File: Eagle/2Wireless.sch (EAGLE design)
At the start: 21 parts, among them IC1 TCA9517A, IC2 VREGLD1117, IC3 MB85RS2MTAPNF-G-BDERE1, IC4 24FC512, IC5 24FC512, U1 PHOTON_WITH_HEADERS

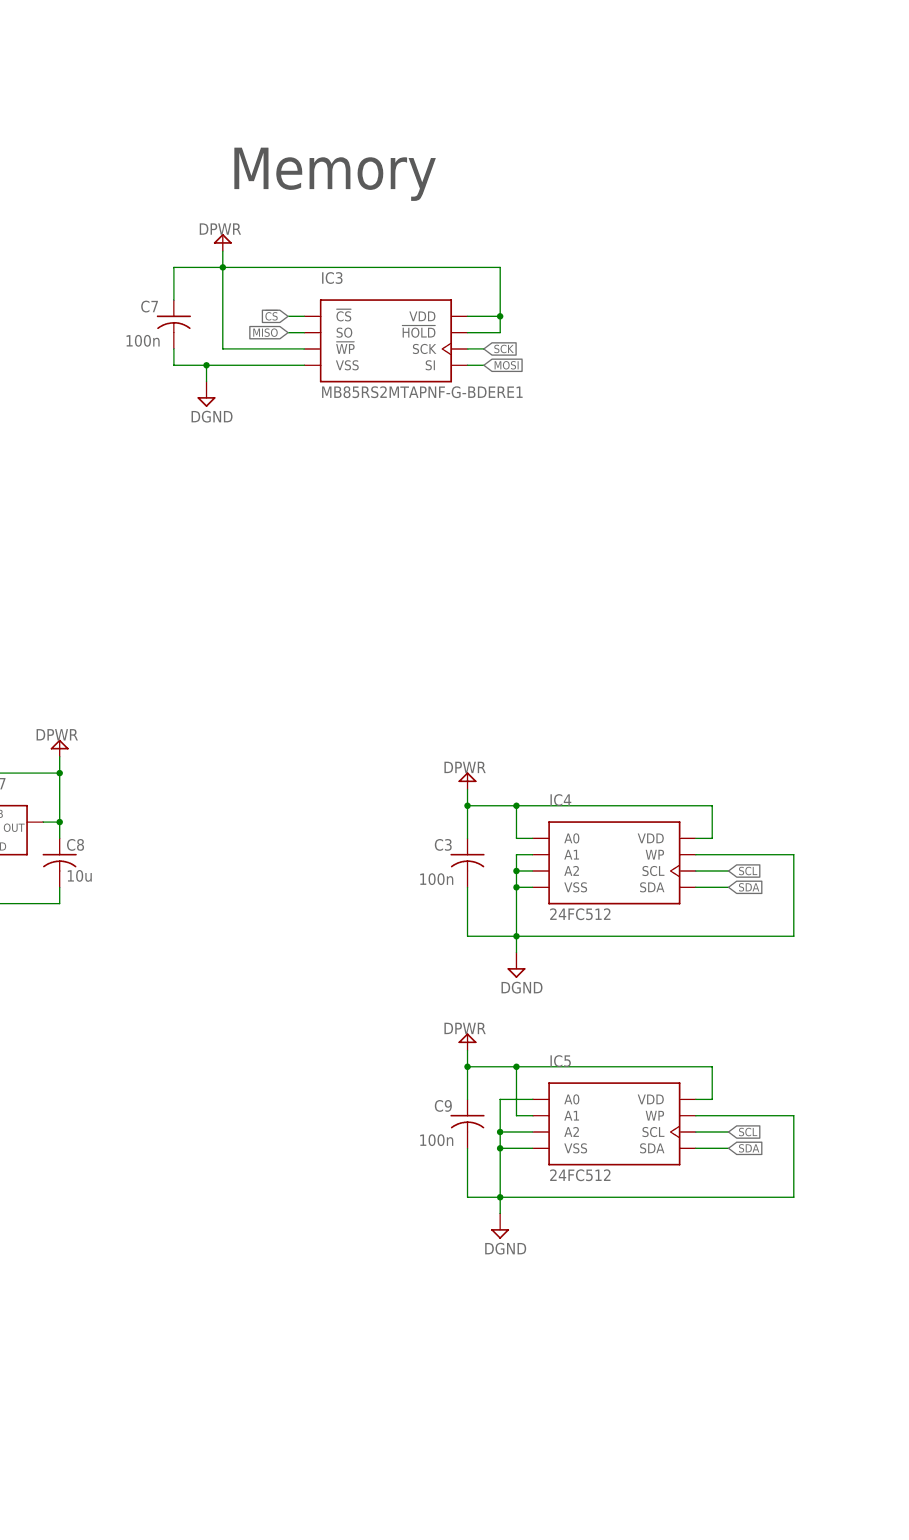
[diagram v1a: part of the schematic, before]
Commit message: Add two more 24FC512.
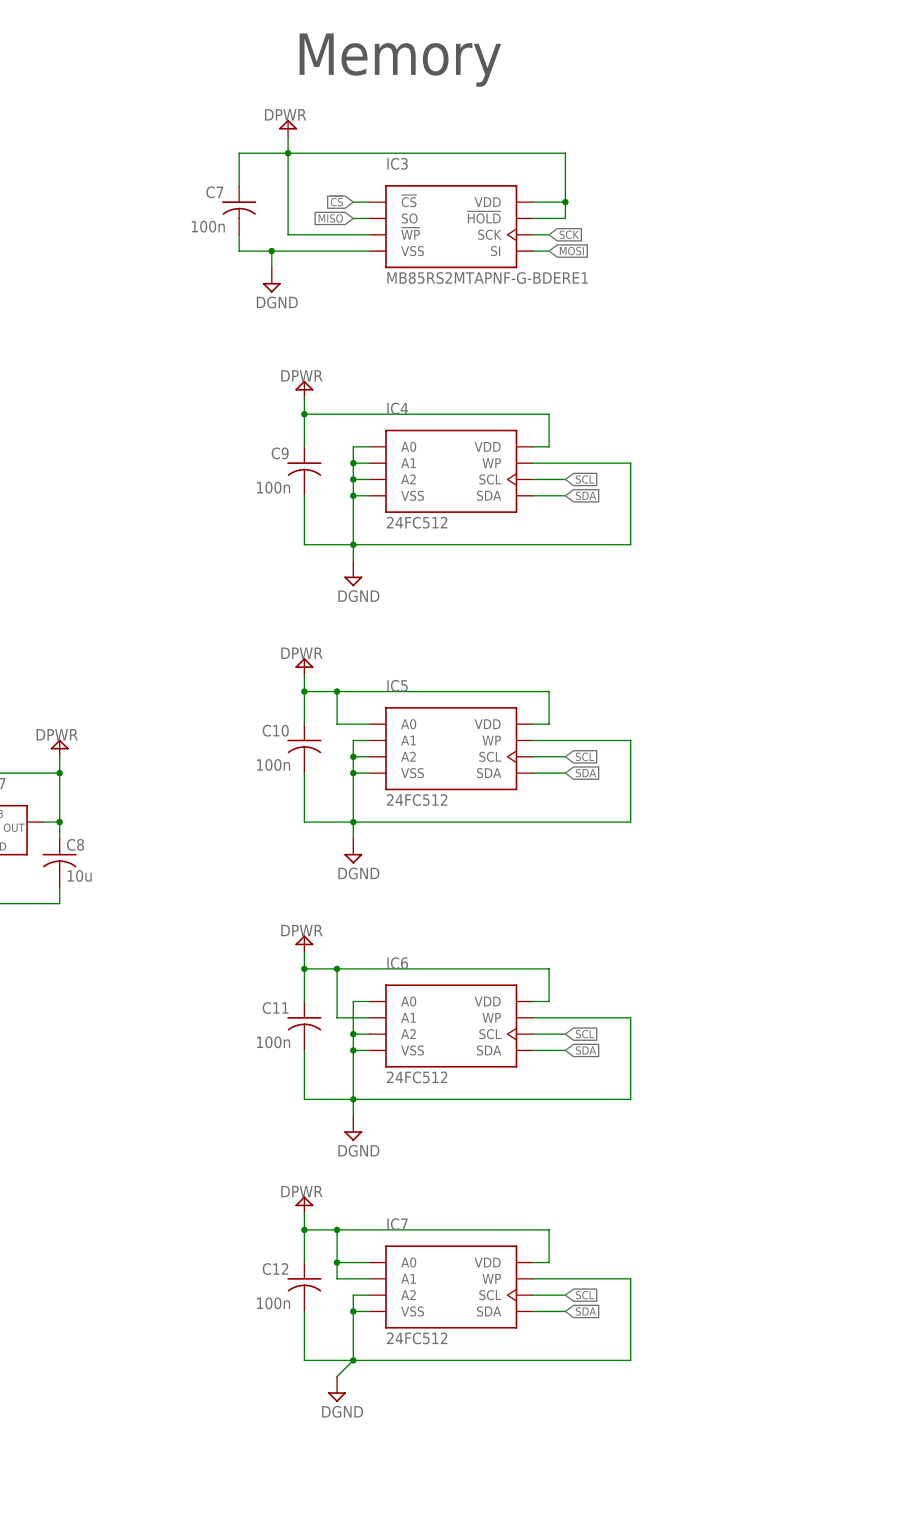
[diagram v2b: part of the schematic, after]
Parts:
- removed C3: 100n, studio_h:CB
- added C10, C11, C12: 100n, studio_h:CB
- added IC6, IC7: 24FC512, studio_h:FRAM24FC512
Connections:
- net DGND: now also C10.2, C11.2, C12.2, IC4.A0, IC5.A1, IC6.A0, IC6.A2, IC6.VSS, IC6.WP, IC7.A2, IC7.VSS, IC7.WP; no longer C3.2, IC5.A0
- net DPWR: now also C10.1, C11.1, C12.1, IC5.A0, IC6.A1, IC6.VDD, IC7.A0, IC7.A1, IC7.VDD; no longer C3.1, IC4.A0, IC5.A1
- net SCL: now also IC6.SCL, IC7.SCL
- net SDA: now also IC6.SDA, IC7.SDA
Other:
- moved on the sheet: C7, C9, IC3, IC4, IC5

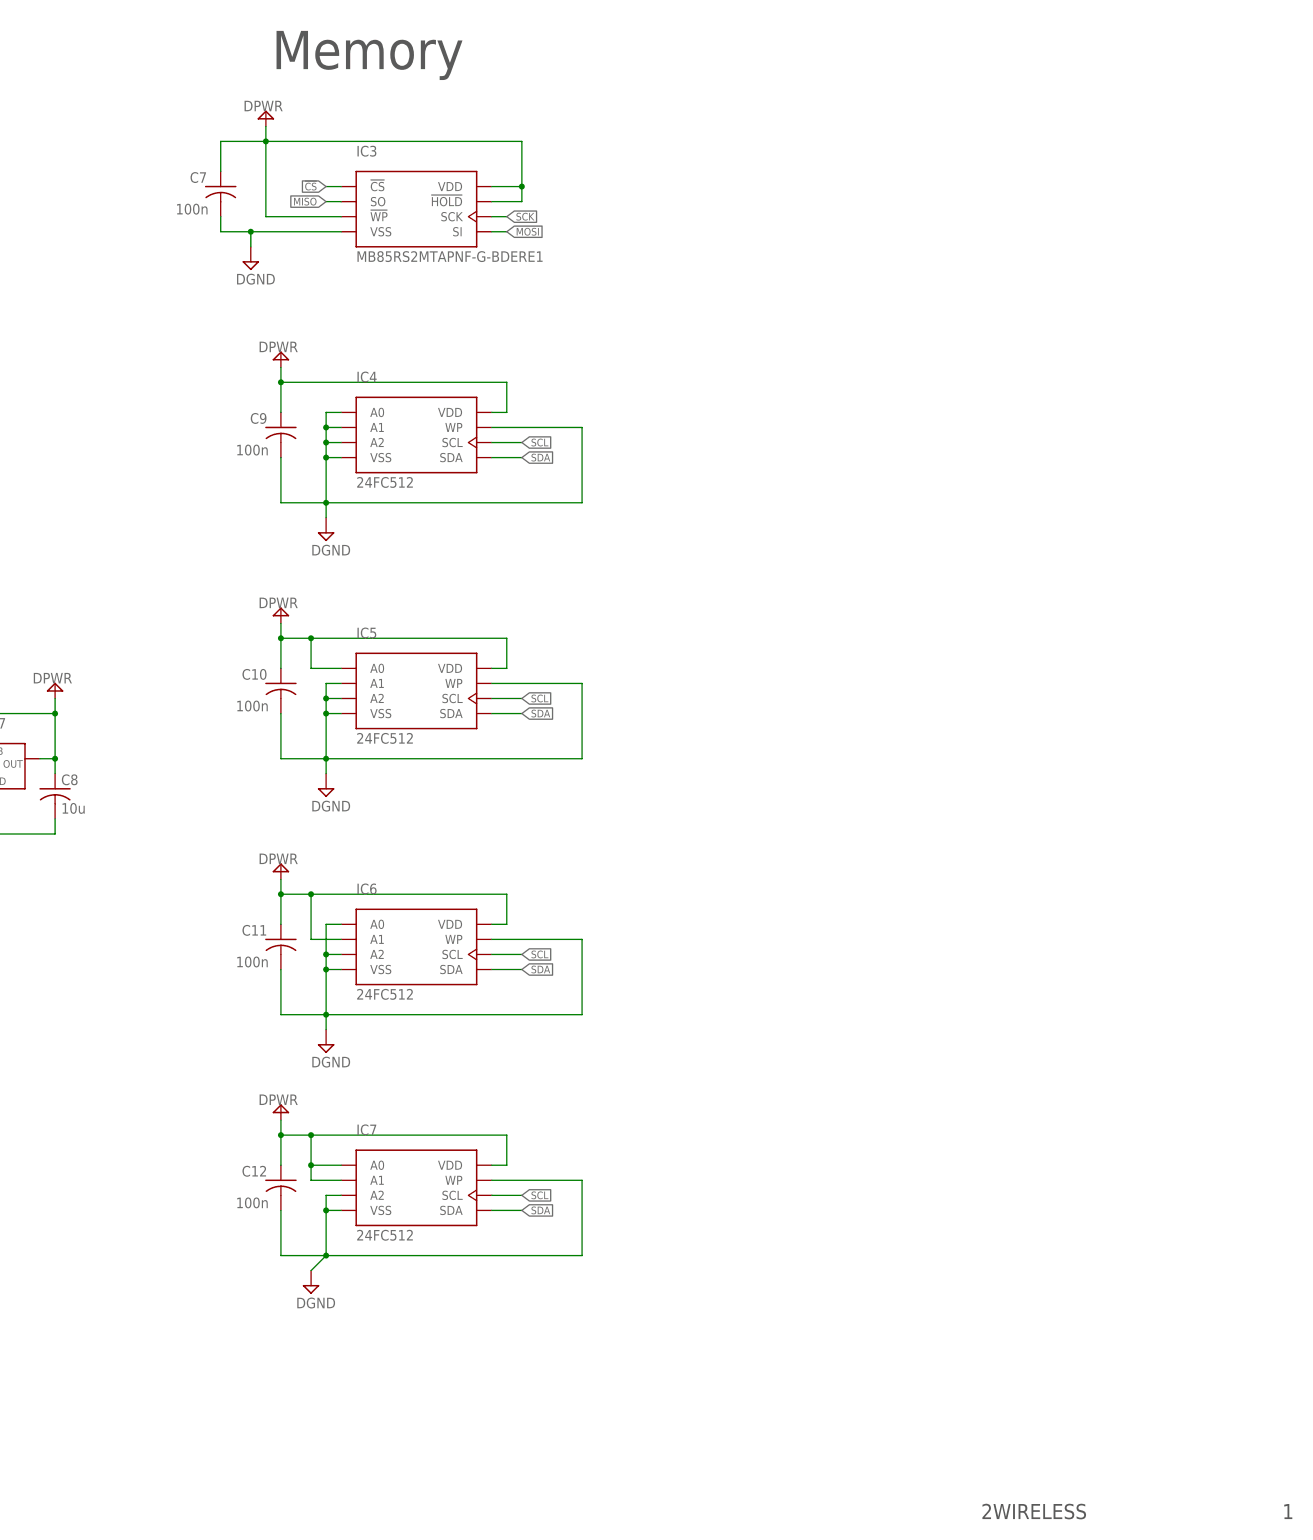
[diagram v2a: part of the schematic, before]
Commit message: Remove 24FC512 chips. Not needed.
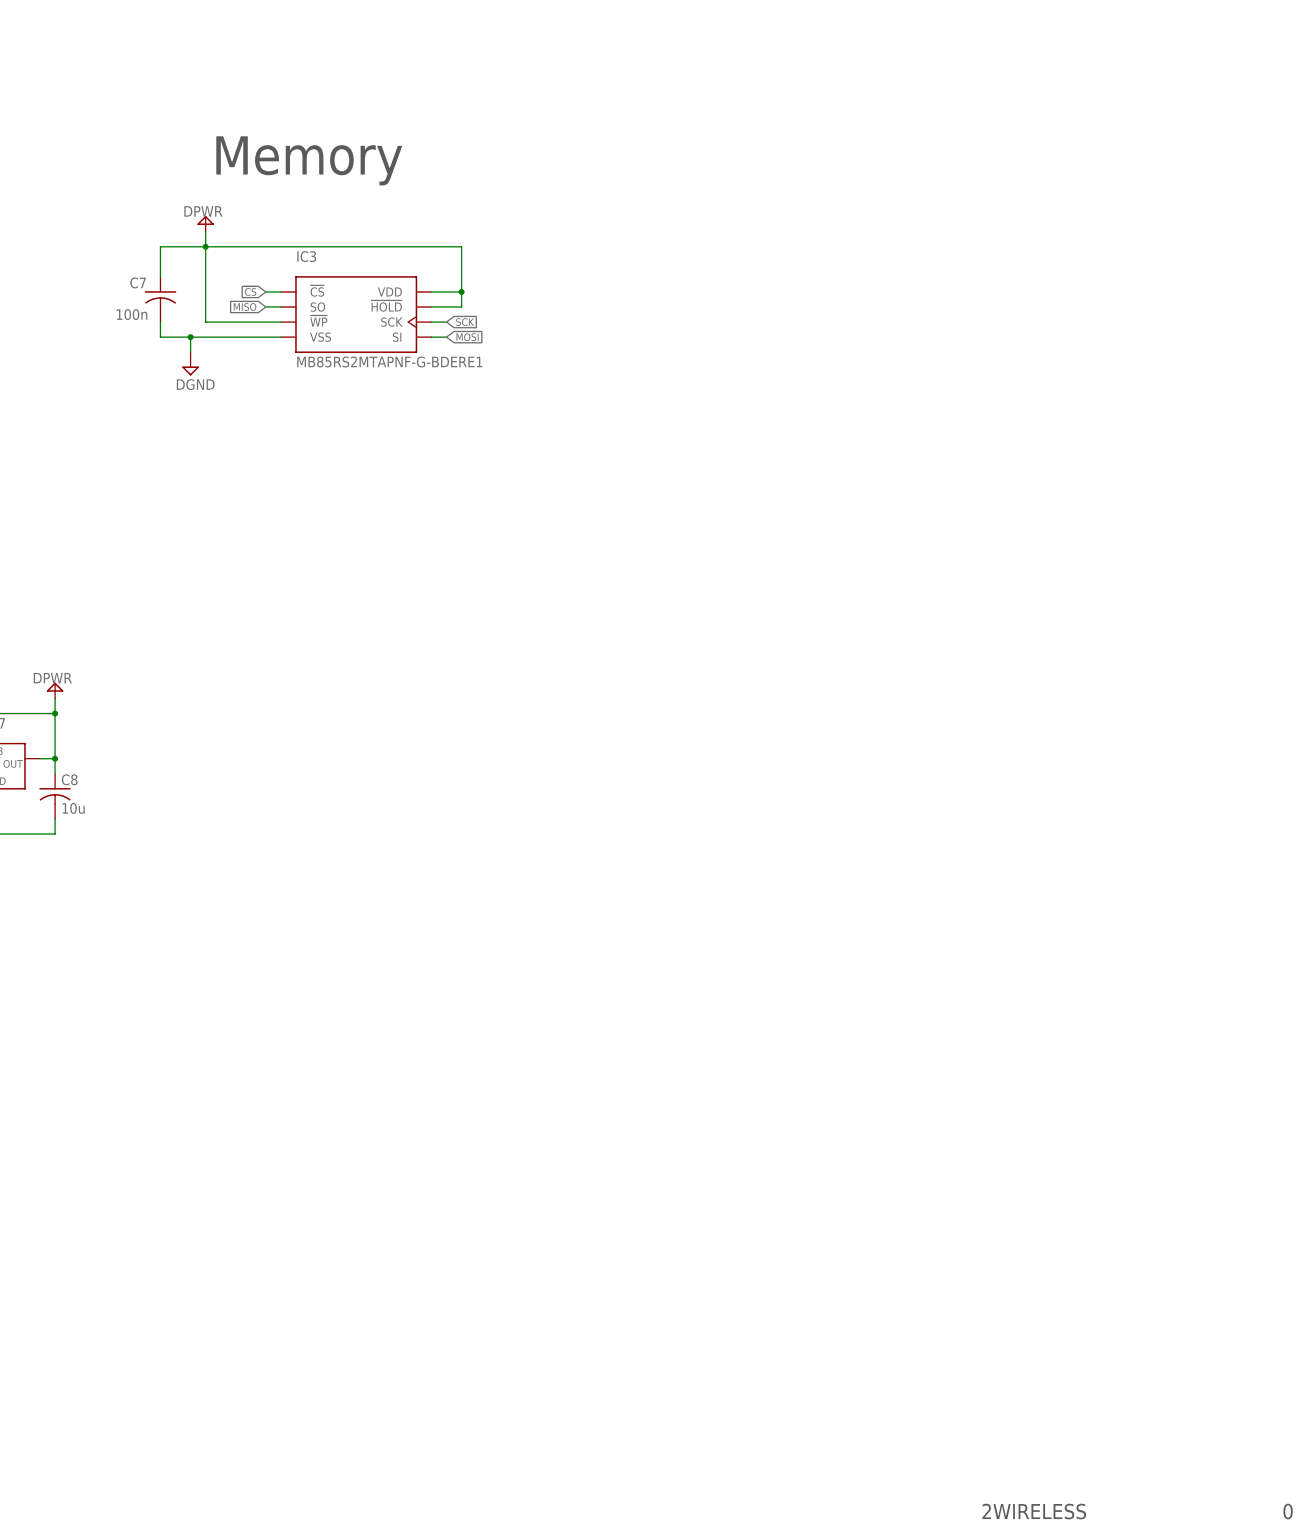
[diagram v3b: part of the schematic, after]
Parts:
- removed C10, C11, C12, C9: 100n, studio_h:CB
- removed IC4, IC5, IC6, IC7: 24FC512, studio_h:FRAM24FC512
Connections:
- net DGND: no longer C10.2, C11.2, C12.2, C9.2, IC4.A0, IC4.A1, IC4.A2, IC4.VSS, IC4.WP, IC5.A1, IC5.A2, IC5.VSS, IC5.WP, IC6.A0, IC6.A2, IC6.VSS, IC6.WP, IC7.A2, IC7.VSS, IC7.WP
- net DPWR: no longer C10.1, C11.1, C12.1, C9.1, IC4.VDD, IC5.A0, IC5.VDD, IC6.A1, IC6.VDD, IC7.A0, IC7.A1, IC7.VDD
- net SCL: no longer IC4.SCL, IC5.SCL, IC6.SCL, IC7.SCL
- net SDA: no longer IC4.SDA, IC5.SDA, IC6.SDA, IC7.SDA
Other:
- note added: "0"
- note removed: "1"
- moved on the sheet: C7, IC3
